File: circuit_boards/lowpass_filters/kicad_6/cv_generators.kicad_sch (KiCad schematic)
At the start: 28 parts, among them U6 TL072, U7 TL072

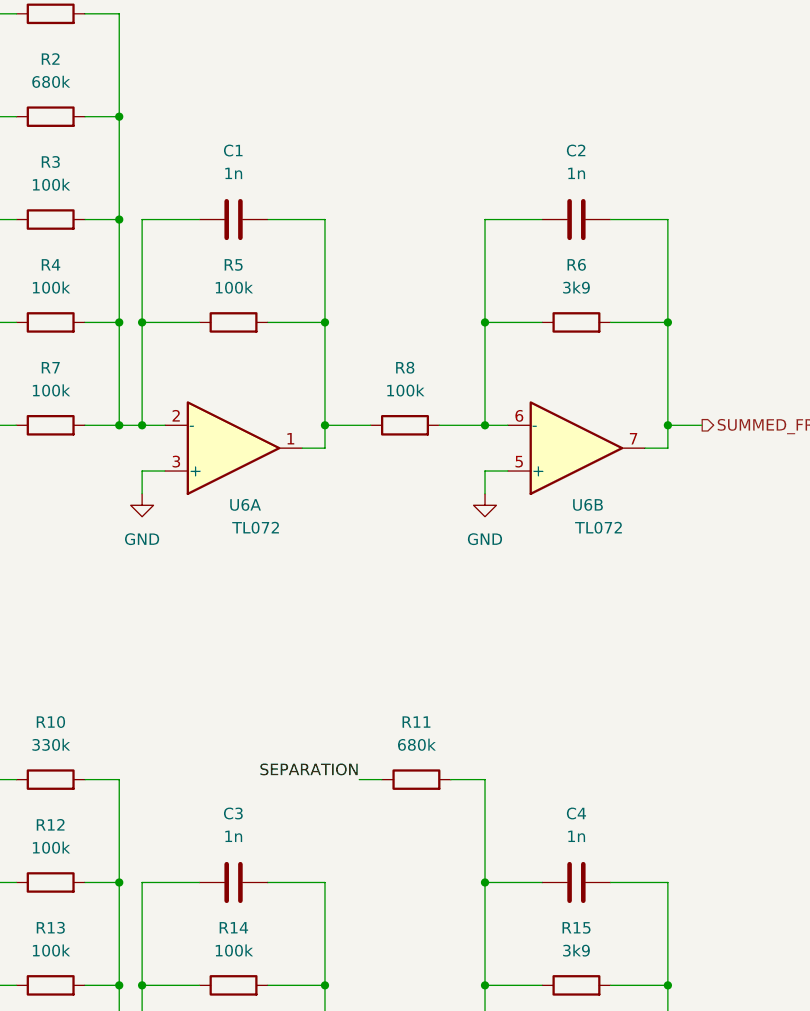
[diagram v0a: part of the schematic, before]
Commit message: Update PCB files, fix VCF mix polarity
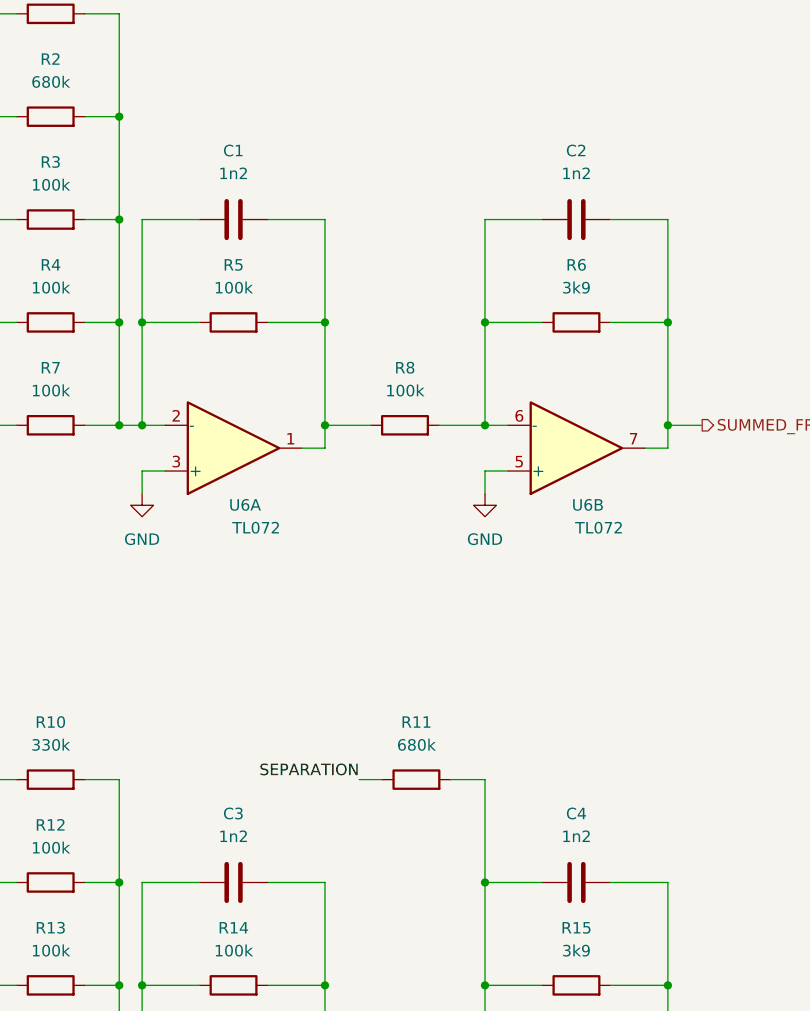
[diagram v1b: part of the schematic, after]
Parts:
- C1, C2, C3, C4: value 1n -> 1n2
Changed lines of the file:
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@@
     (in_bom yes) (on_board yes) (fields_autoplaced)
     (property "Reference" "C3" (id 0) (at 142.24 118.11 90))
-    (property "Value" "1n" (id 1) (at 142.24 120.65 90))
+    (property "Value" "1n2" (id 1) (at 142.24 120.65 90))
     (property "Footprint" "Capacitor_SMD:C_0805_2012Metric" (id 2) (at 146.05 124.7648 0)
       (effects (font (size 1.27 1.27)) hide)
@@
     (in_bom yes) (on_board yes) (fields_autoplaced)
     (property "Reference" "C2" (id 0) (at 180.34 44.45 90))
-    (property "Value" "1n" (id 1) (at 180.34 46.99 90))
+    (property "Value" "1n2" (id 1) (at 180.34 46.99 90))
     (property "Footprint" "Capacitor_SMD:C_0805_2012Metric" (id 2) (at 184.15 51.1048 0)
       (effects (font (size 1.27 1.27)) hide)
@@
     (in_bom yes) (on_board yes) (fields_autoplaced)
     (property "Reference" "C4" (id 0) (at 180.34 118.11 90))
-    (property "Value" "1n" (id 1) (at 180.34 120.65 90))
+    (property "Value" "1n2" (id 1) (at 180.34 120.65 90))
     (property "Footprint" "Capacitor_SMD:C_0805_2012Metric" (id 2) (at 184.15 124.7648 0)
       (effects (font (size 1.27 1.27)) hide)
@@
     (in_bom yes) (on_board yes) (fields_autoplaced)
     (property "Reference" "C1" (id 0) (at 142.24 44.45 90))
-    (property "Value" "1n" (id 1) (at 142.24 46.99 90))
+    (property "Value" "1n2" (id 1) (at 142.24 46.99 90))
     (property "Footprint" "Capacitor_SMD:C_0805_2012Metric" (id 2) (at 146.05 51.1048 0)
       (effects (font (size 1.27 1.27)) hide)
